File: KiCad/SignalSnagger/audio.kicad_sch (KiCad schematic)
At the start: 66 parts, among them J301 Headphones, J302 36-5005-ND, J303 36-5005-ND, J304 36-5006-ND, U301 LM386, U302 TS912IDT, U303 TS912IDT, U304 LM386

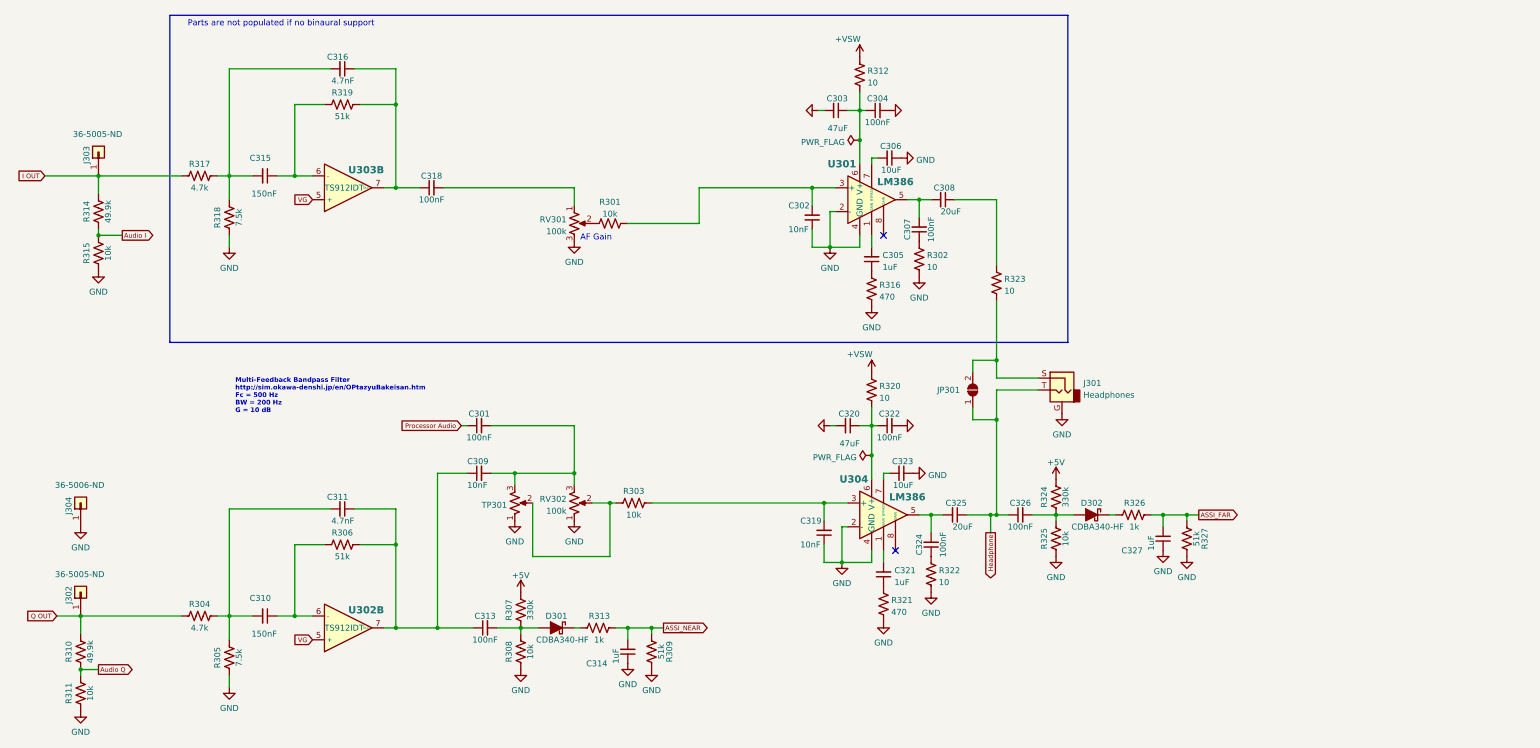
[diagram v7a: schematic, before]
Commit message: Schematic Updates
Adding part numbers and footprints
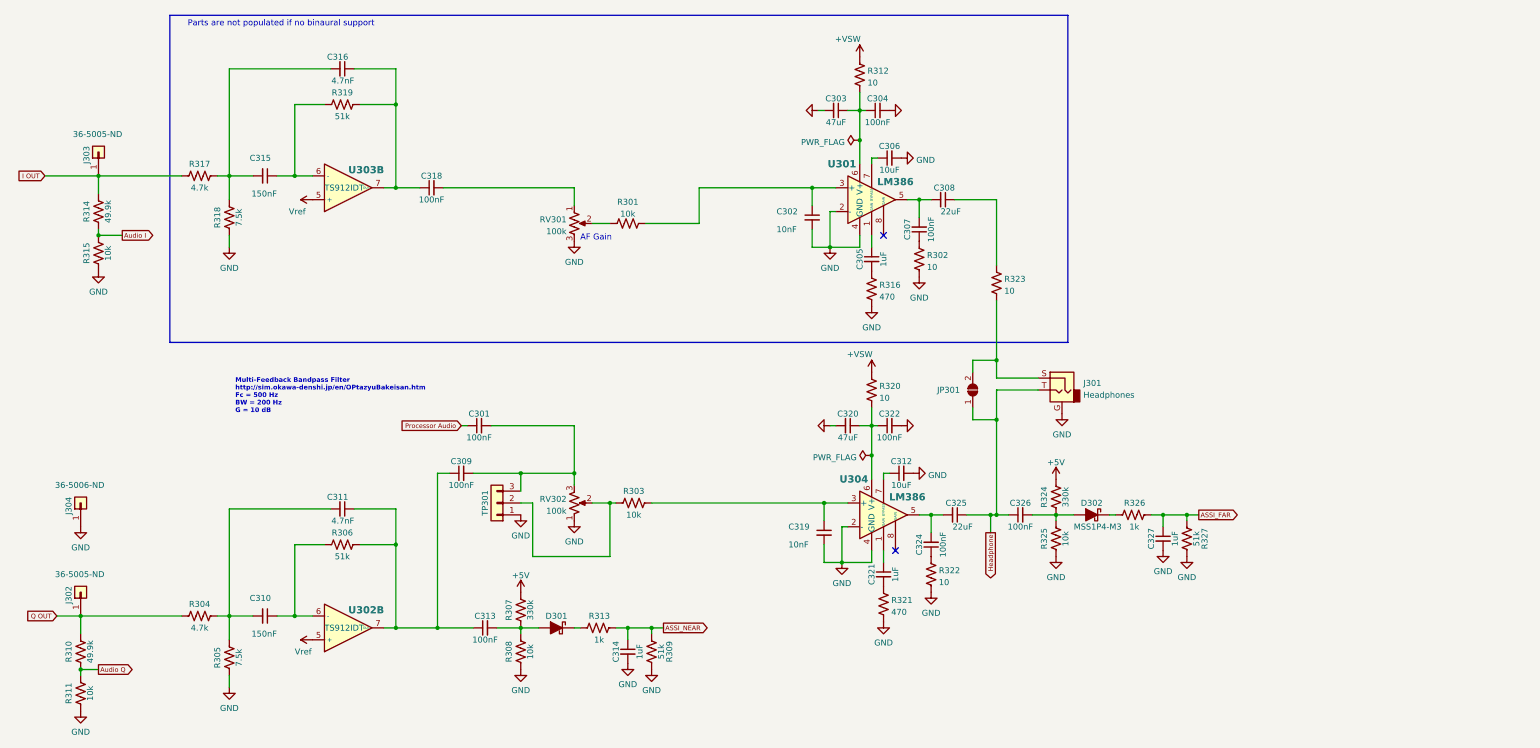
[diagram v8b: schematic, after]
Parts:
- removed C323: 10uF, symbol Device:C_Small
- removed TP301: 100k, Connector_PinHeader_2.54mm:PinHeader_1x03_P2.54mm_Vertical, symbol Device:R_Potentiometer_US
- added C312: 10uF, Capacitor_SMD:C_0603_1608Metric, symbol Device:C_Small
- added TP301: Conn_01x03, Connector_PinHeader_2.54mm:PinHeader_1x03_P2.54mm_Vertical, symbol Connector_Generic:Conn_01x03
- C302, C319: footprint (none) -> Capacitor_SMD:C_0603_1608Metric; Digi-Key Part No. (none) -> 399-C0603X103J4HACAUTOCT-ND; Link (none) -> https://www.digikey.com/short/w78125d0; Manufacturer (none) -> KEMET; Manufacturer PN (none) -> C0603X103J4HACAUTO
- C303, C320: footprint (none) -> Capacitor_SMD:C_1210_3225Metric; Digi-Key Part No. (none) -> 1276-3376-1-ND; Manufacturer (none) -> Samsung Electro-Mechanics; Manufacturer PN (none) -> CL32A476KOJNNNE
- C305, C314, C321, C327: footprint (none) -> Capacitor_SMD:C_0201_0603Metric; Digi-Key Part No. (none) -> 311-1445-1-ND; LCSC Part Number (none) -> C29926; Link (none) -> https://www.digikey.com/short/q2f22qnq; Manufacturer (none) -> YAGEO; Manufacturer PN (none) -> CC0603KRX5R8BB105
- C306: footprint (none) -> Capacitor_SMD:C_0603_1608Metric; Digi-Key Part No. (none) -> 1276-1006-1-ND; Link (none) -> https://www.digikey.com/en/products/detail/samsung-electro-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; Manufacturer (none) -> Samsung Electro-Mechanics; Manufacturer PN (none) -> CL10B104KA8NNNC
- C308, C325: value 20uF -> 22uF; footprint (none) -> Capacitor_SMD:C_0805_2012Metric; Digi-Key Part No. (none) -> 1276-2909-1-ND; Manufacturer (none) -> Samsung Electro-Mechanics; Manufacturer PN (none) -> CL21A226MOQNNNE
- C309: value 10nF -> 100nF; footprint (none) -> Capacitor_SMD:C_0603_1608Metric; Digi-Key Part No. (none) -> 1276-1006-1-ND; Link (none) -> https://www.digikey.com/en/products/detail/samsung-electro-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; Manufacturer (none) -> Samsung Electro-Mechanics; Manufacturer PN (none) -> CL10B104KA8NNNC
- C310, C315: footprint (none) -> Capacitor_SMD:C_0603_1608Metric; Digi-Key Part No. (none) -> 399-C0603C154J4RAC7867CT-ND; Manufacturer (none) -> KEMET; Manufacturer PN (none) -> C0603C154J4RAC7867
- C311, C316: footprint (none) -> Capacitor_SMD:C_0603_1608Metric; Digi-Key Part No. (none) -> 399-17879-1-ND; Manufacturer (none) -> KEMET; Manufacturer PN (none) -> C0603C472K4RECAUTO
- D301: value CDBA340-HF -> (none); footprint Diode_SMD:D_SMA -> (none); Digi-Key Part No. (none) -> MSS1P4-M3/89AGICT-ND; Manufacturer (none) -> Vishay General Semiconductor - Diodes Division; Manufacturer PN (none) -> MSS1P4-M3/89A
- D302: value CDBA340-HF -> MSS1P4-M3; footprint Diode_SMD:D_SMA -> Diode_SMD:DO-219AD; Digi-Key Part No. (none) -> MSS1P4-M3/89AGICT-ND; Manufacturer (none) -> Vishay General Semiconductor - Diodes Division; Manufacturer PN (none) -> MSS1P4-M3/89A
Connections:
- net ASSI_FAR: now also C327.1; no longer C327.2
- net ASSI_NEAR: now also C314.1; no longer C314.2
- net GND: now also C302.2, C306.2, C314.2, C319.2, C327.2, C312.2, TP301.1 (Pin_1); no longer C302.1, C306.1, C314.1, C319.1, C327.1
- net at R301.2, U301.3 (+): now also C302.1; no longer C302.2
- net at U304.1 (GAIN): now also C321.1; no longer C321.2
- net at R303.2, U304.3 (+): now also C319.1; no longer C319.2
- net at U304.7 (BYPASS): now also C312.1
- net at U301.1 (GAIN): now also C305.1; no longer C305.2
- net at U301.7 (BYPASS): now also C306.1; no longer C306.2
- net at R321.1: now also C321.2; no longer C321.1
- net at R303.1, RV302.2: now also TP301.2 (Pin_2)
- net at C301.2, C309.2, RV302.3: now also TP301.3 (Pin_3)
- net at R316.1: now also C305.2; no longer C305.1
- net VG renamed Vref
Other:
- moved on the sheet: R301
